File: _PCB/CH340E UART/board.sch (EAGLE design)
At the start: 11 parts, among them IC1 REG1117, U1 CH340ESMD

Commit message: CH340e design complete
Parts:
- removed D1: 1206size, SparkFun-LED:LED1206
- removed J1: (no value), SparkFun-Connectors:USB_MICRO-B_SMT
- added LED1: (no value), adafruit:LEDCHIPLED_0805
- added USB2: ST-USB-001G, Seeed-Connector:MICRO-USB-SMD-B-WITHOUT-POST-W/P(ST-USB-001G)
- JP1: value JUMPER-SMT_3_1-NC_PASTE_SILK -> JUMPER-SMT_3_NO_SILK; device SparkFun-Jumpers:JUMPER-SMT_3_1-NC_PASTE_SILK -> SparkFun-Jumpers:JUMPER-SMT_3_NO_SILK
- renumbered U1 to CH340E
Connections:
- net 5V1 renamed 3V3
- net 5V: now also USB2.VCC; no longer J1.VBUS
- net GND: now also LED1.C, USB2.GND@1, USB2.GND@2, USB2.GND@3, USB2.GND@4, USB2.GND@5; no longer D1.C, J1.GND
- net N$1: now also LED1.A; no longer D1.A
- net USBN: now also USB2.DM; no longer J1.D-
- net USBP: now also USB2.DP; no longer J1.D+

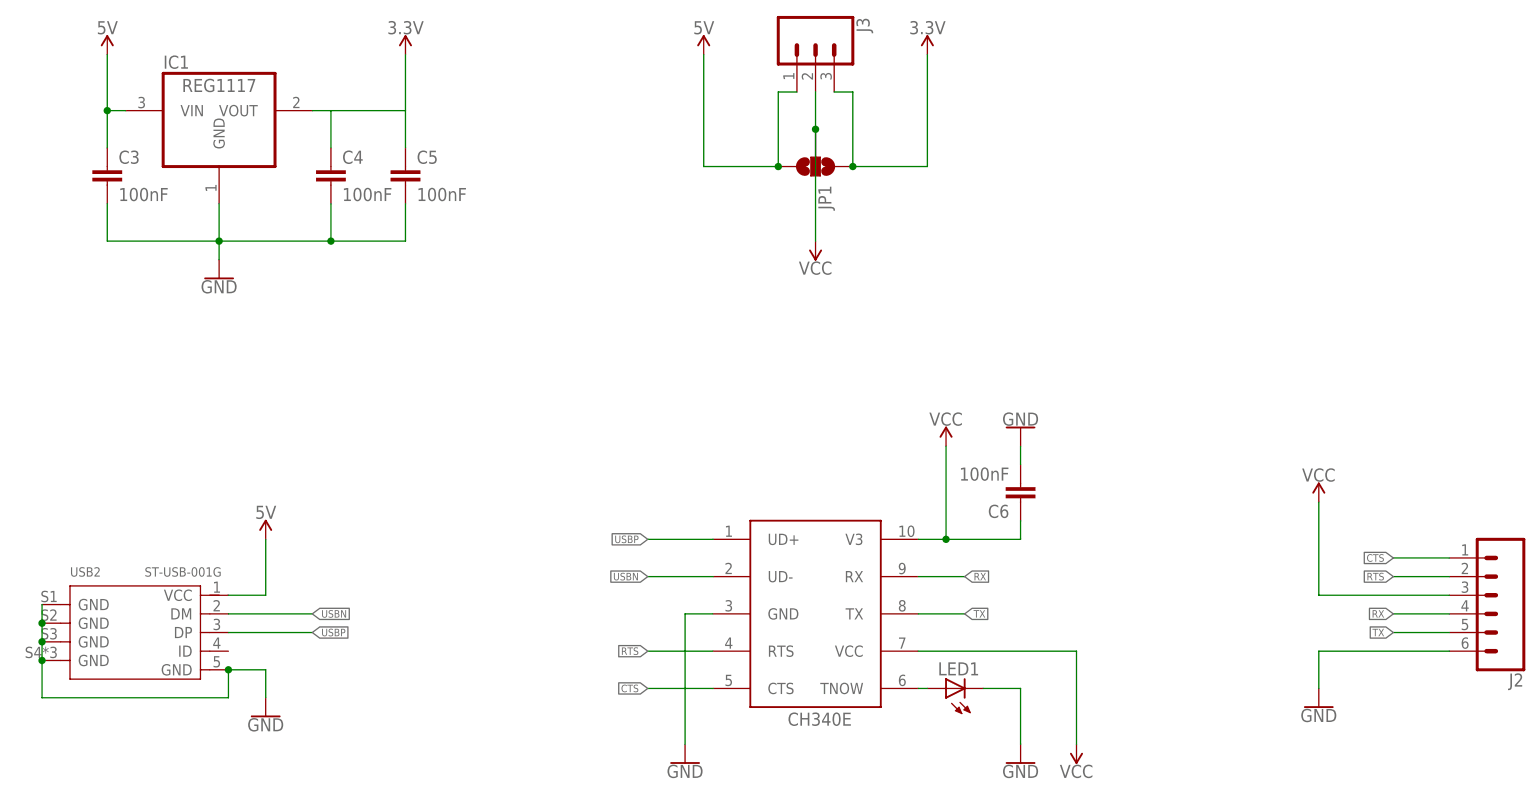
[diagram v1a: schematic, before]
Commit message: CH340E converter complete + LoRa sensor node
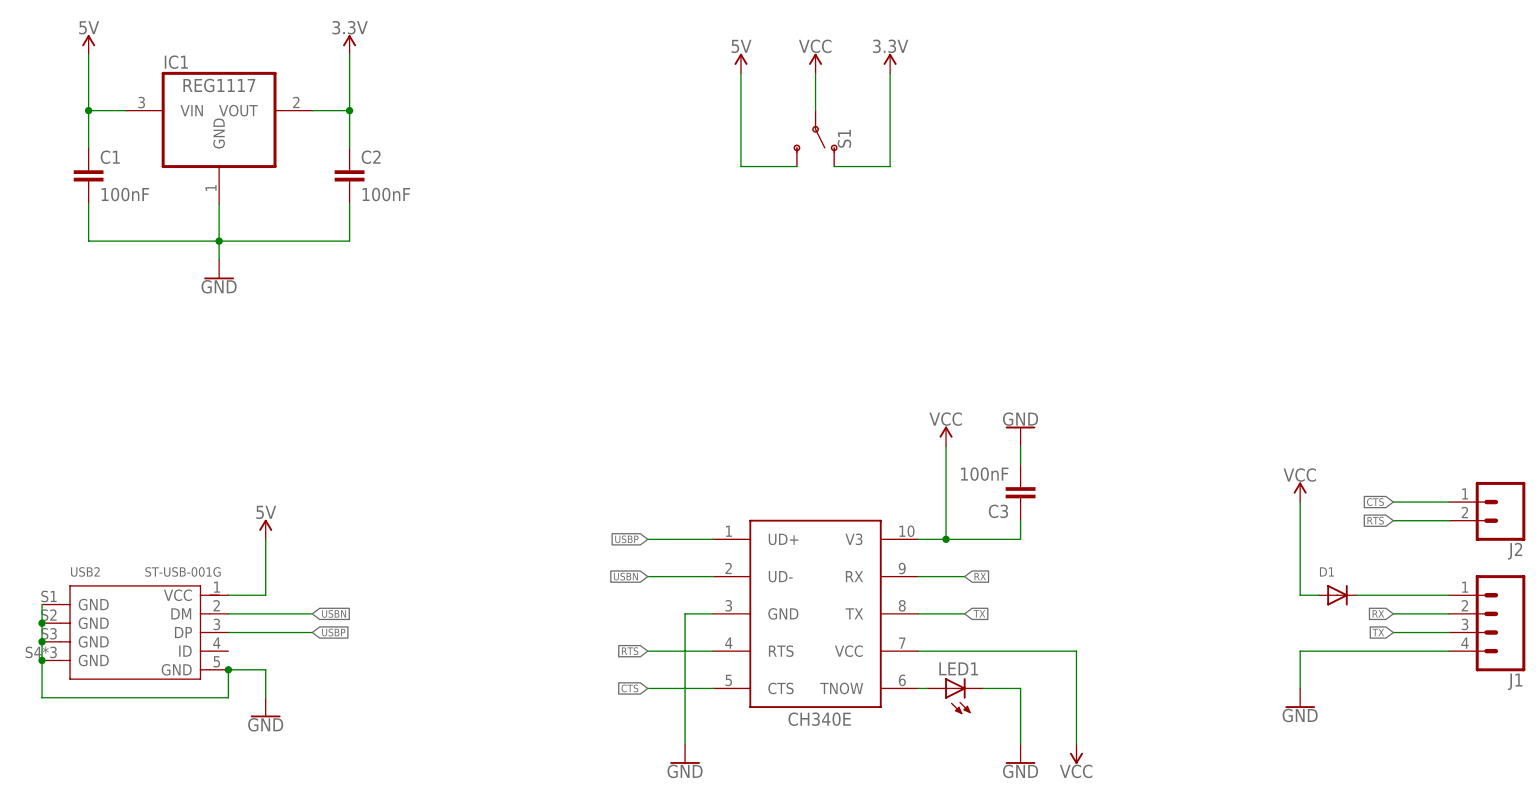
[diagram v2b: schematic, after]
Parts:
- removed C4, C5, C6: 100nF, rcl-2:C-EUC0805
- removed J3: (no value), SparkFun-Connectors:CONN_03
- removed JP1: JUMPER-SMT_3_NO_SILK, SparkFun-Jumpers:JUMPER-SMT_3_NO_SILK
- added C1, C2: 100nF, rcl-2:C-EUC0805
- added D1: (no value), adafruit:DIODESOD-323F
- added J1: (no value), SparkFun-Connectors:CONN_04
- added S1: (no value), SparkFun-Switches:SWITCH-SPDT-SMD-RIGHT-ANGLE
- J2: device SparkFun-Connectors:CONN_06SILK_FEMALE_PTH -> SparkFun-Connectors:CONN_02
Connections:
- new net VCC_D: D1.C, J1.1
- net 3.3V: now also S1.O; no longer J3.3, JP1.1
- net 3V3: now also C2.1; no longer C4.1, C5.1
- net 5V: now also C1.1, S1.S; no longer C3.1, J3.1, JP1.3
- net GND: now also C1.2, C2.2, J1.4; no longer C4.2, C5.2, C6.2, J2.6
- net RX: now also J1.2; no longer J2.4
- net TX: now also J1.3; no longer J2.5
- net VCC: now also C3.1, D1.A, S1.P; no longer C6.1, J2.3, J3.2, JP1.2
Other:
- moved on the sheet: C3
